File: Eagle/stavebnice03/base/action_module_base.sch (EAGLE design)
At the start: 7 parts

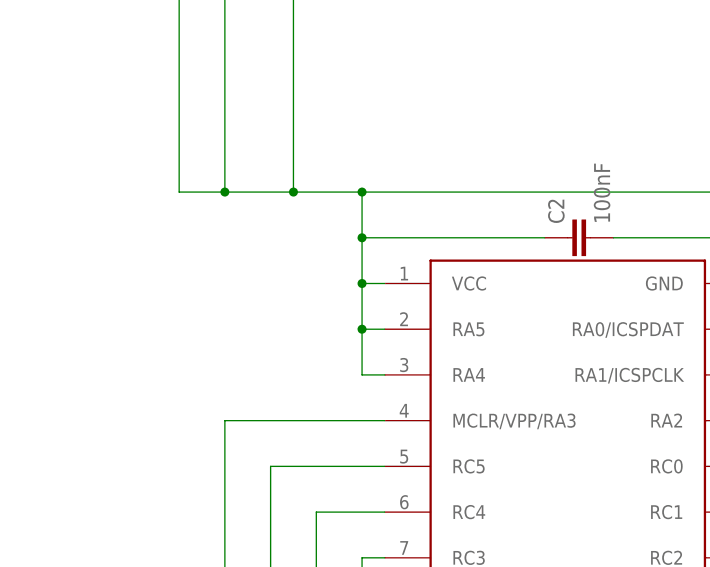
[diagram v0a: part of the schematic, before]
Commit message: added pin and resistor to stay in bootloader + changed size back to 21x21 mm
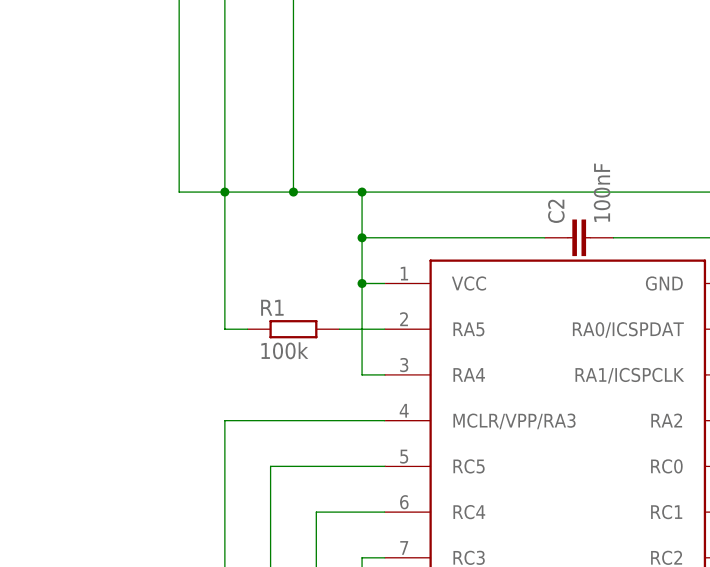
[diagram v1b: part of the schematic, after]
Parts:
- added R1: 100k, resistor:R-EU_R0603
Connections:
- new net N$3: R1.2, U$1.RA5
- net VCC: now also R1.1; no longer U$1.RA5
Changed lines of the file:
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@@
 <layer number="97" name="Info" color="7" fill="1" visible="yes" active="yes"/>
 <layer number="98" name="Guide" color="6" fill="1" visible="yes" active="yes"/>
+<layer number="99" name="SpiceOrder" color="5" fill="1" visible="no" active="no"/>
 </layers>
 <schematic xreflabel="%F%N/%S.%C%R" xrefpart="/%S.%C%R">
@@
 <part name="R3" library="resistor" deviceset="R-EU_" device="R0603" value="2K2"/>
 <part name="R4" library="resistor" deviceset="R-EU_" device="R0603" value="2k2"/>
+<part name="R1" library="resistor" deviceset="R-EU_" device="R0603" value="100k"/>
 </parts>
 <sheets>
@@
 <instance part="R3" gate="G$1" x="106.68" y="144.78" rot="R270"/>
 <instance part="R4" gate="G$1" x="114.3" y="144.78" rot="R270"/>
+<instance part="R1" gate="G$1" x="114.3" y="93.98"/>
 </instances>
 <busses>
@@
 <pinref part="U$1" gate="G$1" pin="RA4"/>
 <wire x1="124.46" y1="88.9" x2="121.92" y2="88.9" width="0.1524" layer="91"/>
-<wire x1="121.92" y1="88.9" x2="121.92" y2="93.98" width="0.1524" layer="91"/>
-<pinref part="U$1" gate="G$1" pin="RA5"/>
-<wire x1="121.92" y1="93.98" x2="121.92" y2="99.06" width="0.1524" layer="91"/>
-<wire x1="124.46" y1="93.98" x2="121.92" y2="93.98" width="0.1524" layer="91"/>
+<wire x1="121.92" y1="88.9" x2="121.92" y2="99.06" width="0.1524" layer="91"/>
 <junction x="121.92" y="99.06"/>
-<junction x="121.92" y="93.98"/>
 <pinref part="R4" gate="G$1" pin="2"/>
 <wire x1="114.3" y1="139.7" x2="114.3" y2="109.22" width="0.1524" layer="91"/>
@@
 <wire x1="106.68" y1="109.22" x2="106.68" y2="139.7" width="0.1524" layer="91"/>
 <junction x="106.68" y="109.22"/>
+<pinref part="R1" gate="G$1" pin="1"/>
+<wire x1="109.22" y1="93.98" x2="106.68" y2="93.98" width="0.1524" layer="91"/>
+<wire x1="106.68" y1="93.98" x2="106.68" y2="109.22" width="0.1524" layer="91"/>
 </segment>
 </net>
@@
 </segment>
 </net>
+<net name="N$3" class="0">
+<segment>
+<pinref part="U$1" gate="G$1" pin="RA5"/>
+<pinref part="R1" gate="G$1" pin="2"/>
+<wire x1="124.46" y1="93.98" x2="119.38" y2="93.98" width="0.1524" layer="91"/>
+</segment>
+</net>

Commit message: C0603 changed to C0603K with wider space between soldering areas
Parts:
- C2: device resistor:C-EUC0603 -> resistor:C-EUC0603K
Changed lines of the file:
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@@
 <parts>
 <part name="U$1" library="!stavebnice03" deviceset="16F103-TSSOP" device=""/>
-<part name="C2" library="resistor" deviceset="C-EU" device="C0603" value="100nF"/>
+<part name="C2" library="resistor" deviceset="C-EU" device="C0603K" value="100nF"/>
 <part name="U$4" library="!stavebnice03" deviceset="JUMPER5M-90" device=""/>
 <part name="U$8" library="!stavebnice03" deviceset="JUMPER6M" device=""/>

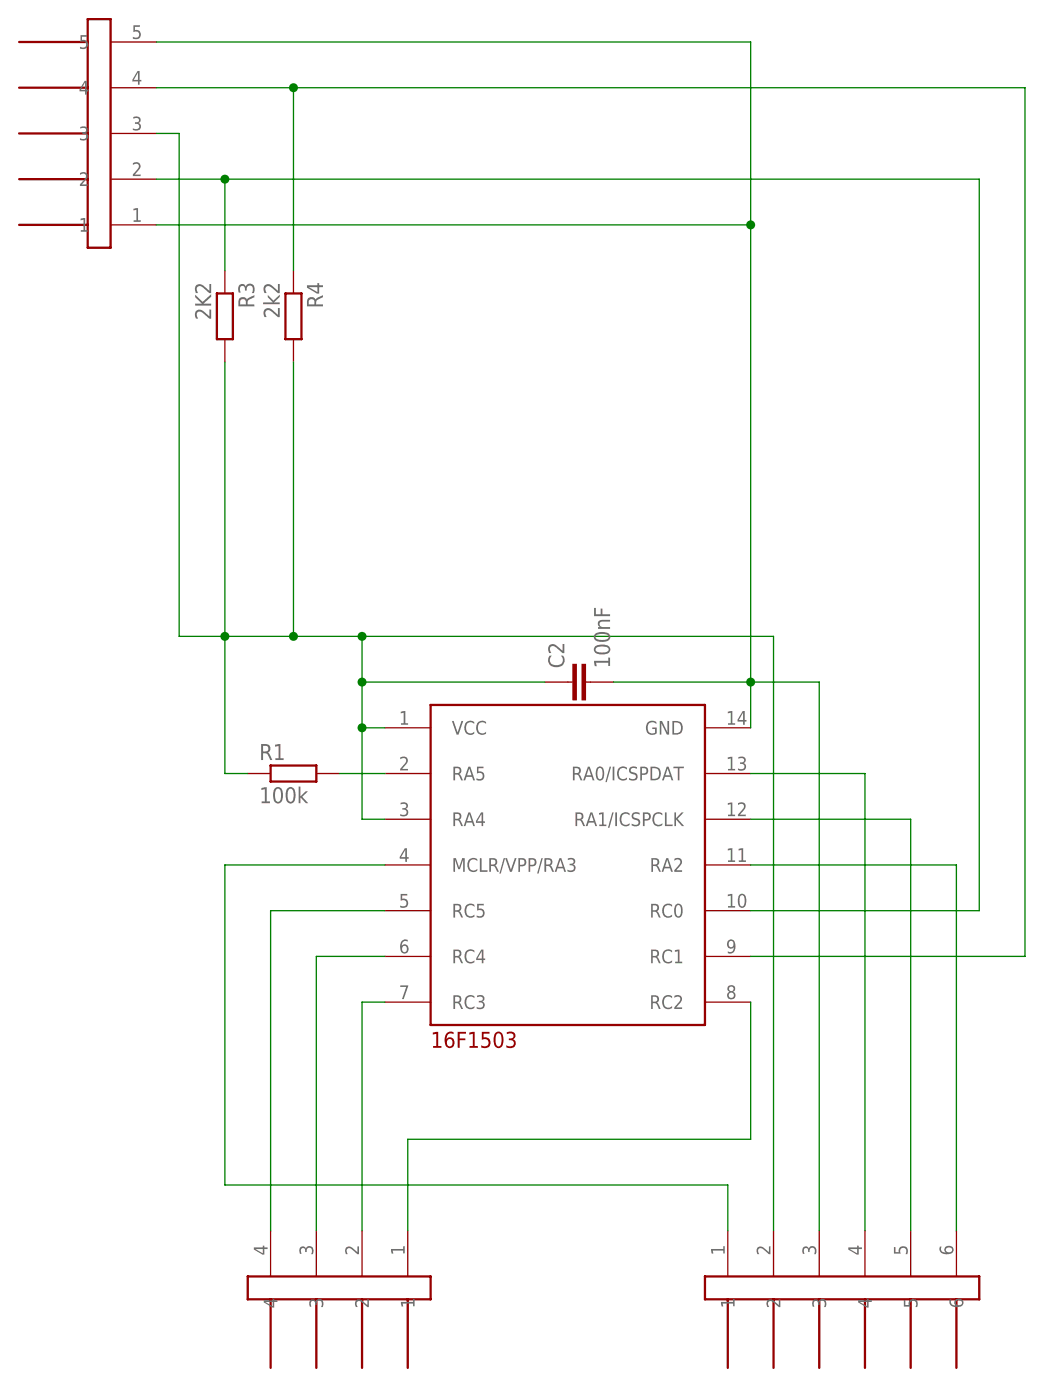
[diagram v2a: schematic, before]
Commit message: element position changed to be able put the bords to boxes + reset button for source board
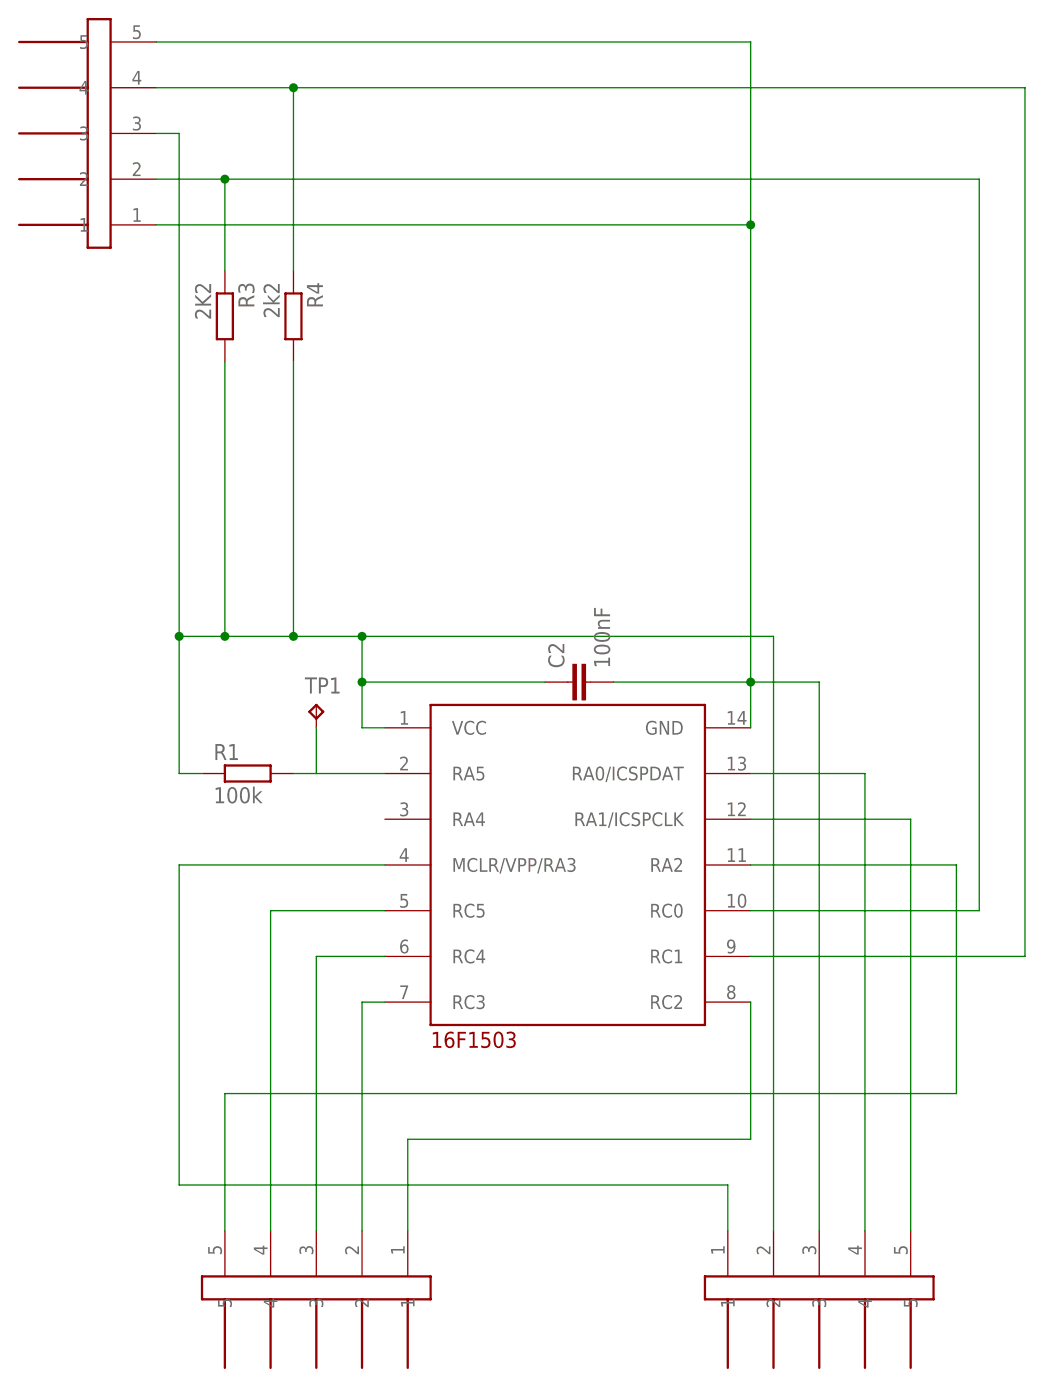
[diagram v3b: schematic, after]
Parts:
- removed U$8: JUMPER6M, !stavebnice03:JUMPER6M
- removed U$9: JUMPER4M, !stavebnice03:JUMPER4M
- added TP1: TPB1,27, testpad:TPB1,27
- added U$2, U$3: JUMPER5M, !stavebnice03:JUMPER5M
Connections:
- net GND: now also U$2.3; no longer U$8.3
- net N$1: now also U$3.2; no longer U$9.2
- net N$11: now also U$3.5; no longer U$8.6
- net N$12: now also U$3.4; no longer U$9.4
- net N$13: now also U$2.1; no longer U$8.1
- net N$14: now also U$2.4; no longer U$8.4
- net N$15: now also U$2.5; no longer U$8.5
- net N$17: now also U$3.3; no longer U$9.3
- net N$18: now also U$3.1; no longer U$9.1
- net N$3: now also TP1.TP
- net VCC: now also U$2.2; no longer U$1.RA4, U$8.2
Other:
- moved on the sheet: R1
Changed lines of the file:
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@@
 <part name="C2" library="resistor" deviceset="C-EU" device="C0603K" value="100nF"/>
 <part name="U$4" library="!stavebnice03" deviceset="JUMPER5M-90" device=""/>
-<part name="U$8" library="!stavebnice03" deviceset="JUMPER6M" device=""/>
-<part name="U$9" library="!stavebnice03" deviceset="JUMPER4M" device=""/>
 <part name="R3" library="resistor" deviceset="R-EU_" device="R0603" value="2K2"/>
 <part name="R4" library="resistor" deviceset="R-EU_" device="R0603" value="2k2"/>
 <part name="R1" library="resistor" deviceset="R-EU_" device="R0603" value="100k"/>
+<part name="U$2" library="!stavebnice03" deviceset="JUMPER5M" device=""/>
+<part name="U$3" library="!stavebnice03" deviceset="JUMPER5M" device=""/>
+<part name="TP1" library="testpad" deviceset="TP" device="B1,27"/>
 </parts>
 <sheets>
@@
 <instance part="C2" gate="G$1" x="144.78" y="104.14" rot="R90"/>
 <instance part="U$4" gate="G$1" x="91.44" y="165.1" rot="R180"/>
-<instance part="U$8" gate="G$1" x="175.26" y="35.56" rot="MR270"/>
-<instance part="U$9" gate="G$1" x="119.38" y="35.56" rot="R270"/>
 <instance part="R3" gate="G$1" x="106.68" y="144.78" rot="R270"/>
 <instance part="R4" gate="G$1" x="114.3" y="144.78" rot="R270"/>
-<instance part="R1" gate="G$1" x="114.3" y="93.98"/>
+<instance part="R1" gate="G$1" x="109.22" y="93.98"/>
+<instance part="U$2" gate="G$1" x="172.72" y="35.56" rot="MR270"/>
+<instance part="U$3" gate="G$1" x="116.84" y="35.56" rot="R270"/>
+<instance part="TP1" gate="G$1" x="116.84" y="101.6"/>
 </instances>
 <busses>
@@
 <pinref part="C2" gate="G$1" pin="2"/>
 <wire x1="149.86" y1="104.14" x2="165.1" y2="104.14" width="0.1524" layer="91"/>
-<pinref part="U$8" gate="G$1" pin="3"/>
+<pinref part="U$2" gate="G$1" pin="3"/>
 </segment>
 </net>
@@
 <wire x1="121.92" y1="109.22" x2="114.3" y2="109.22" width="0.1524" layer="91"/>
 <wire x1="114.3" y1="109.22" x2="106.68" y2="109.22" width="0.1524" layer="91"/>
-<wire x1="106.68" y1="109.22" x2="101.6" y2="109.22" width="0.1524" layer="91"/>
 <wire x1="101.6" y1="109.22" x2="101.6" y2="165.1" width="0.1524" layer="91"/>
 <wire x1="101.6" y1="165.1" x2="99.06" y2="165.1" width="0.1524" layer="91"/>
@@
 <junction x="121.92" y="104.14"/>
 <pinref part="U$4" gate="G$1" pin="3"/>
-<pinref part="U$8" gate="G$1" pin="2"/>
-<pinref part="U$1" gate="G$1" pin="RA4"/>
-<wire x1="124.46" y1="88.9" x2="121.92" y2="88.9" width="0.1524" layer="91"/>
-<wire x1="121.92" y1="88.9" x2="121.92" y2="99.06" width="0.1524" layer="91"/>
-<junction x="121.92" y="99.06"/>
 <pinref part="R4" gate="G$1" pin="2"/>
 <wire x1="114.3" y1="139.7" x2="114.3" y2="109.22" width="0.1524" layer="91"/>
@@
 <junction x="106.68" y="109.22"/>
 <pinref part="R1" gate="G$1" pin="1"/>
-<wire x1="109.22" y1="93.98" x2="106.68" y2="93.98" width="0.1524" layer="91"/>
-<wire x1="106.68" y1="93.98" x2="106.68" y2="109.22" width="0.1524" layer="91"/>
+<wire x1="104.14" y1="93.98" x2="101.6" y2="93.98" width="0.1524" layer="91"/>
+<wire x1="101.6" y1="93.98" x2="101.6" y2="109.22" width="0.1524" layer="91"/>
+<wire x1="101.6" y1="109.22" x2="106.68" y2="109.22" width="0.1524" layer="91"/>
+<pinref part="U$2" gate="G$1" pin="2"/>
+<junction x="101.6" y="109.22"/>
 </segment>
 </net>
@@
 <segment>
 <wire x1="162.56" y1="43.18" x2="162.56" y2="48.26" width="0.1524" layer="91"/>
-<wire x1="162.56" y1="48.26" x2="106.68" y2="48.26" width="0.1524" layer="91"/>
-<wire x1="106.68" y1="48.26" x2="106.68" y2="83.82" width="0.1524" layer="91"/>
+<wire x1="162.56" y1="48.26" x2="101.6" y2="48.26" width="0.1524" layer="91"/>
+<wire x1="101.6" y1="48.26" x2="101.6" y2="83.82" width="0.1524" layer="91"/>
 <pinref part="U$1" gate="G$1" pin="MCLR/VPP/RA3"/>
-<wire x1="106.68" y1="83.82" x2="124.46" y2="83.82" width="0.1524" layer="91"/>
-<pinref part="U$8" gate="G$1" pin="1"/>
+<wire x1="101.6" y1="83.82" x2="124.46" y2="83.82" width="0.1524" layer="91"/>
+<pinref part="U$2" gate="G$1" pin="1"/>
 </segment>
 </net>
@@
 <wire x1="177.8" y1="93.98" x2="165.1" y2="93.98" width="0.1524" layer="91"/>
 <pinref part="U$1" gate="G$1" pin="RA0/ICSPDAT"/>
-<pinref part="U$8" gate="G$1" pin="4"/>
+<pinref part="U$2" gate="G$1" pin="4"/>
 </segment>
 </net>
@@
 <wire x1="165.1" y1="88.9" x2="182.88" y2="88.9" width="0.1524" layer="91"/>
 <wire x1="182.88" y1="88.9" x2="182.88" y2="43.18" width="0.1524" layer="91"/>
-<pinref part="U$8" gate="G$1" pin="5"/>
+<pinref part="U$2" gate="G$1" pin="5"/>
 </segment>
 </net>
@@
 <pinref part="U$1" gate="G$1" pin="RA2"/>
 <wire x1="165.1" y1="83.82" x2="187.96" y2="83.82" width="0.1524" layer="91"/>
-<wire x1="187.96" y1="83.82" x2="187.96" y2="43.18" width="0.1524" layer="91"/>
-<pinref part="U$8" gate="G$1" pin="6"/>
+<wire x1="187.96" y1="83.82" x2="187.96" y2="58.42" width="0.1524" layer="91"/>
+<wire x1="187.96" y1="58.42" x2="106.68" y2="58.42" width="0.1524" layer="91"/>
+<wire x1="106.68" y1="58.42" x2="106.68" y2="43.18" width="0.1524" layer="91"/>
+<pinref part="U$3" gate="G$1" pin="5"/>
 </segment>
 </net>
@@
 <pinref part="U$1" gate="G$1" pin="RC2"/>
 <wire x1="165.1" y1="53.34" x2="165.1" y2="68.58" width="0.1524" layer="91"/>
-<pinref part="U$9" gate="G$1" pin="1"/>
 <wire x1="165.1" y1="53.34" x2="127" y2="53.34" width="0.1524" layer="91"/>
 <wire x1="127" y1="53.34" x2="127" y2="43.18" width="0.1524" layer="91"/>
+<pinref part="U$3" gate="G$1" pin="1"/>
 </segment>
 </net>
@@
 <pinref part="U$1" gate="G$1" pin="RC4"/>
 <wire x1="124.46" y1="73.66" x2="116.84" y2="73.66" width="0.1524" layer="91"/>
-<pinref part="U$9" gate="G$1" pin="3"/>
 <wire x1="116.84" y1="73.66" x2="116.84" y2="43.18" width="0.1524" layer="91"/>
+<pinref part="U$3" gate="G$1" pin="3"/>
 </segment>
 </net>
@@
 <segment>
 <pinref part="U$1" gate="G$1" pin="RC5"/>
-<pinref part="U$9" gate="G$1" pin="4"/>
 <wire x1="124.46" y1="78.74" x2="111.76" y2="78.74" width="0.1524" layer="91"/>
 <wire x1="111.76" y1="78.74" x2="111.76" y2="43.18" width="0.1524" layer="91"/>
+<pinref part="U$3" gate="G$1" pin="4"/>
 </segment>
 </net>
@@
 <net name="N$1" class="0">
 <segment>
-<pinref part="U$9" gate="G$1" pin="2"/>
 <pinref part="U$1" gate="G$1" pin="RC3"/>
 <wire x1="121.92" y1="43.18" x2="121.92" y2="68.58" width="0.1524" layer="91"/>
 <wire x1="121.92" y1="68.58" x2="124.46" y2="68.58" width="0.1524" layer="91"/>
+<pinref part="U$3" gate="G$1" pin="2"/>
 </segment>
 </net>
@@
 <pinref part="U$1" gate="G$1" pin="RA5"/>
 <pinref part="R1" gate="G$1" pin="2"/>
-<wire x1="124.46" y1="93.98" x2="119.38" y2="93.98" width="0.1524" layer="91"/>
+<wire x1="124.46" y1="93.98" x2="116.84" y2="93.98" width="0.1524" layer="91"/>
+<pinref part="TP1" gate="G$1" pin="TP"/>
+<wire x1="116.84" y1="93.98" x2="114.3" y2="93.98" width="0.1524" layer="91"/>
+<wire x1="116.84" y1="99.06" x2="116.84" y2="93.98" width="0.1524" layer="91"/>
 </segment>
 </net>
